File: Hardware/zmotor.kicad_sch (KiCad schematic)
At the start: 38 parts, among them J5 DG301-5-0-04P-12-00AH, Q10 P25B6EB, Q11 P25B6EB, Q12 P25B6EB, Q9 P25B6EB, U6 IRS2005S, U7 IRS2005S, U8 MCP6282

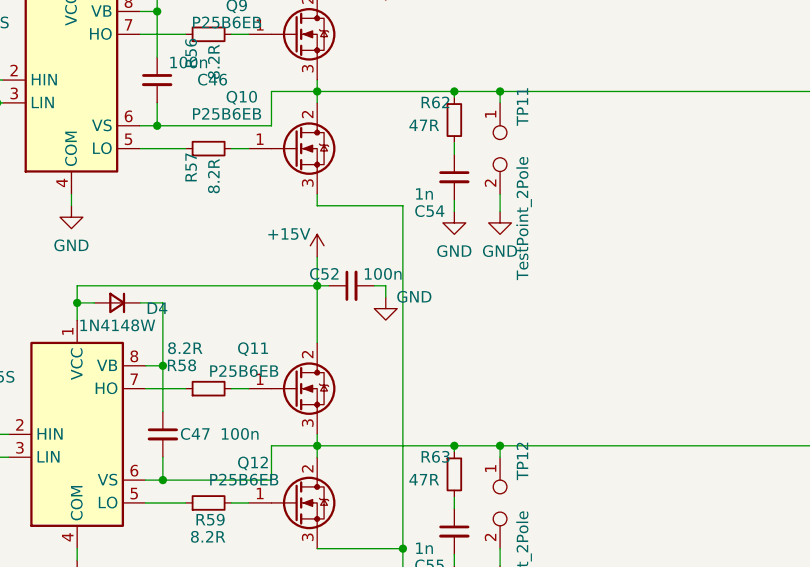
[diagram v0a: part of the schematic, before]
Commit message: Few coonector footprint modifications and silkscreen additions to them.
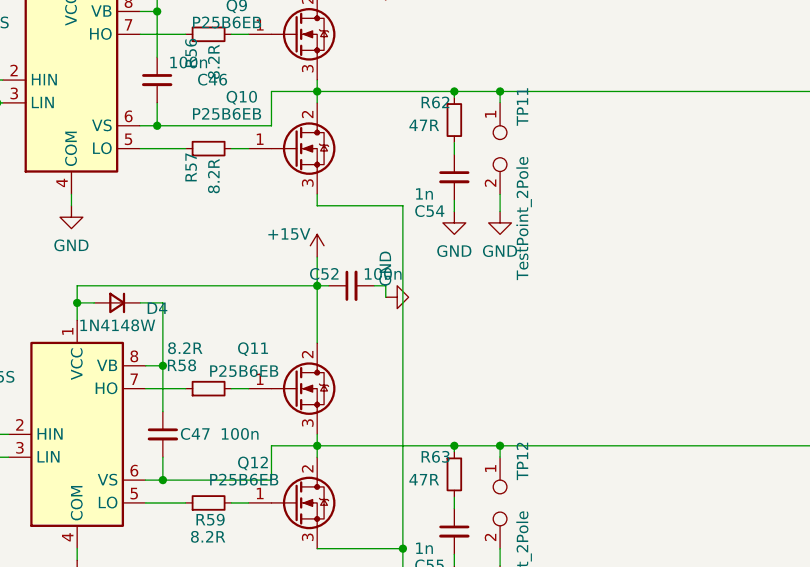
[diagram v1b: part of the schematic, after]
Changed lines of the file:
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@@
     (pin "1")
   )
-  (symbol (lib_id "power:GND") (at 165.735 65.405 0) (unit 1)
+  (symbol (lib_id "power:GND") (at 165.735 65.405 90) (unit 1)
     (in_bom yes) (on_board yes)
-    (property "Reference" "#PWR064" (id 0) (at 165.735 71.755 0)
+    (property "Reference" "#PWR064" (id 0) (at 172.085 65.405 0)
       (effects (font (size 1.27 1.27)) hide)
     )
-    (property "Value" "GND" (id 1) (at 168.91 65.405 0))
+    (property "Value" "GND" (id 1) (at 165.735 62.23 0))
     (property "Footprint" "" (id 2) (at 165.735 65.405 0)
       (effects (font (size 1.27 1.27)) hide)

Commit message: Toolchain set. Timer module added. Schematic files migrated.
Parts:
- C53: value 100n -> 100n
